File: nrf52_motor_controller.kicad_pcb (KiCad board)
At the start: 2 copper layers, 56 x 26.5 mm, 50 parts, among them J1 Screw_Terminal_01x04, J2 Conn_01x12, J3 Conn_01x12, Q1 AO3400A, SW1 SW_Push, SW2 SW_Push, U1 HT7533, U2 nRF52832-QFAA, U3 DRV8876PWPT, Y1 32MHz, Y2 32.768kHz

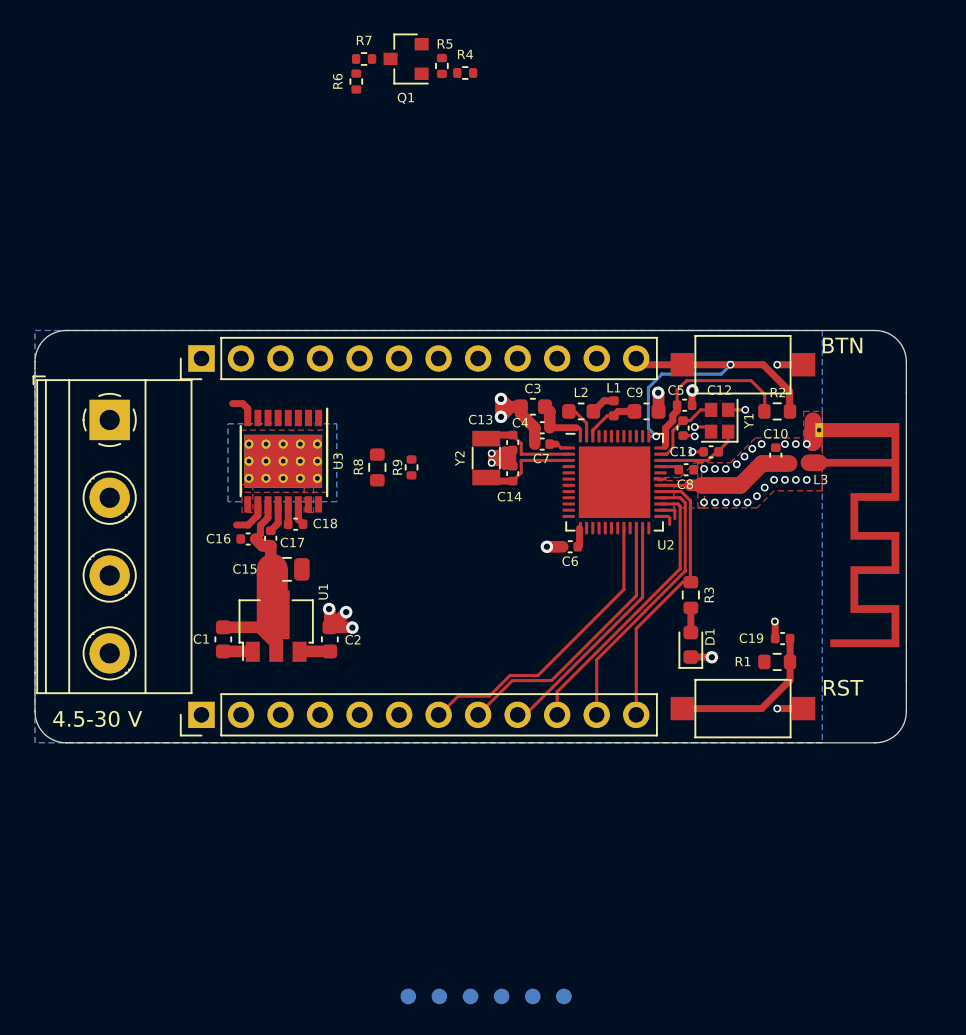
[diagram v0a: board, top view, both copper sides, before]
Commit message: Replace 12 pin headers with 10 pin
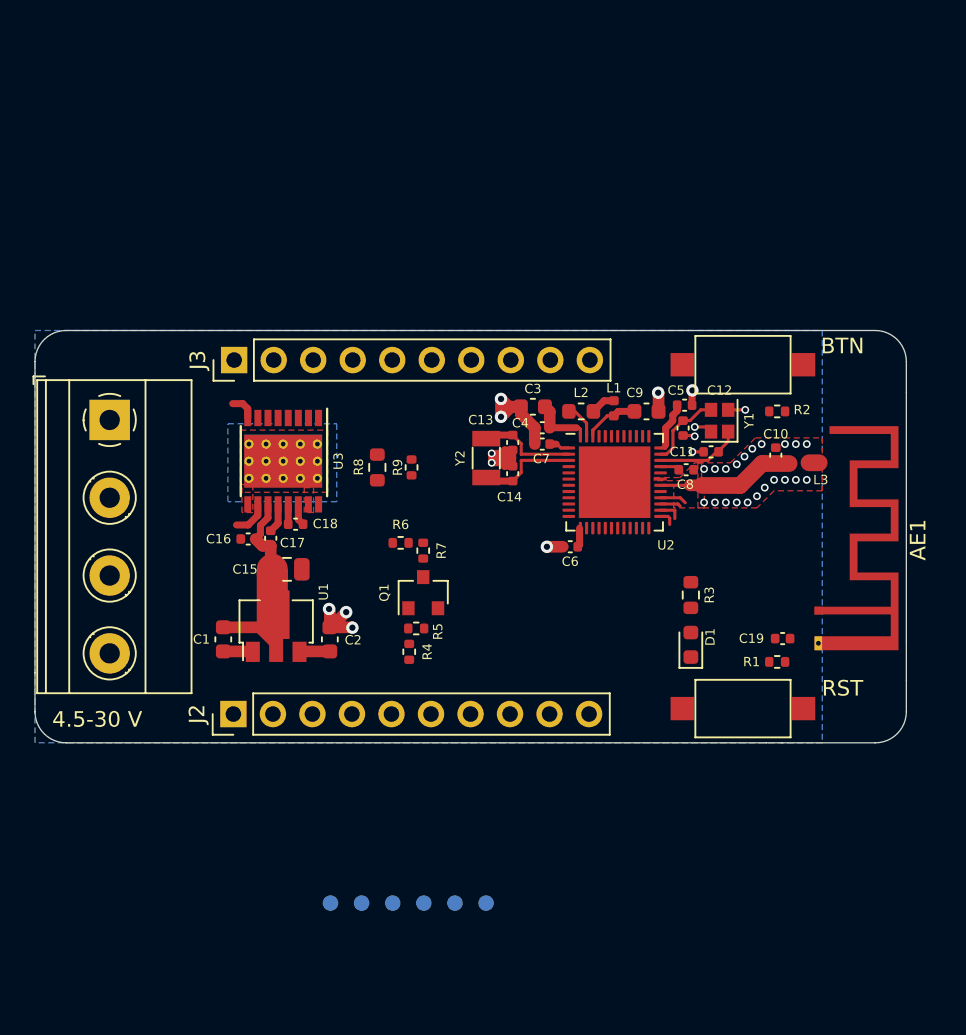
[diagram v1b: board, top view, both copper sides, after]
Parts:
- AE1: footprint RF_Antenna:Texas_SWRA117D_2.4GHz_Right -> RF_Antenna:Texas_SWRA117D_2.4GHz_Left
- J2, J3: value Conn_01x12 -> Conn_01x10; footprint Connector_PinHeader_2.54mm:PinHeader_1x12_P2.54mm_Vertical -> Connector_PinHeader_2.54mm:PinHeader_1x10_P2.54mm_Vertical
- R1, R2: footprint Resistor_SMD:R_0603_1608Metric -> Resistor_SMD:R_0402_1005Metric
- moved R4 37.4 mm to (142.1, 105.7), turned to 270 degrees
- moved R5 36.2 mm to (142.5, 104.2), turned to 0 degrees
- moved Q1 34.3 mm to (142.9, 101.8), turned to 90 degrees
- moved R7 31.8 mm to (142.9, 99.2), turned to 270 degrees
- moved R6 29.8 mm to (141.5, 98.7), turned to 0 degrees
- moved AE1 9.50 mm to (168.3, 103.0)
- moved TP1 7.81 mm to (137.0, 121.8)
- moved TP2 7.81 mm to (139.0, 121.8)
- moved TP3 7.81 mm to (141.0, 121.8)
- moved TP4 7.81 mm to (143.0, 121.8)
- moved TP5 7.81 mm to (145.0, 121.8)
- moved TP6 7.81 mm to (147.0, 121.8)
- moved J3 2.10 mm to (130.8, 86.9)
- moved J2 2.05 mm to (130.8, 109.7)
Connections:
- net /OUT1 renamed /OUT+
- net /OUT2 renamed /OUT-
- J3 pad 10: /GPIO27 -> /GPIO26
- J3 pad 3: (no net) -> /GPIO9
- J3 pad 4: /GPIO9 -> /GPIO10
- J3 pad 5: /GPIO10 -> /GPIO31
- J3 pad 6: /GPIO31 -> /GPIO30
- J3 pad 7: /GPIO30 -> /GPIO29
- J3 pad 8: /GPIO29 -> /GPIO28
- J3 pad 9: /GPIO28 -> /GPIO27
- U2 pad 28: /GPIO23 -> /GPIO_LED
- U2 pad 29: /GPIO_LED -> (no net)
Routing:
- net /GPIO_BTN: track 21.7 -> 0.00 mm, vias 2 -> 0
- net /GPIO17: track 19.2 -> 0.00 mm
- net /GPIO23: track 17.7 -> 0.00 mm
- net /GPIO19: track 17.7 -> 0.00 mm
- net /GPIO22: track 18.0 -> 1.33 mm
- net /GPIO_LED: track 17.7 -> 1.73 mm
- net /GPIO20: track 15.6 -> 0.00 mm
- net /~RESET: track 10.4 -> 0.00 mm
- net GND: track 37.0 -> 28.5 mm, vias 39 -> 35
- net +3V3: track 18.9 -> 10.5 mm
- net Net-(D1-Pad2): track 1.59 -> 0.00 mm
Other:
- board text added: "OUT+"
- board text added: "OUT-"
- board text removed: "OUT1"
- board text removed: "OUT2"

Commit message: Add custom test point symbol and footprint for 1.27 mm pitch TP
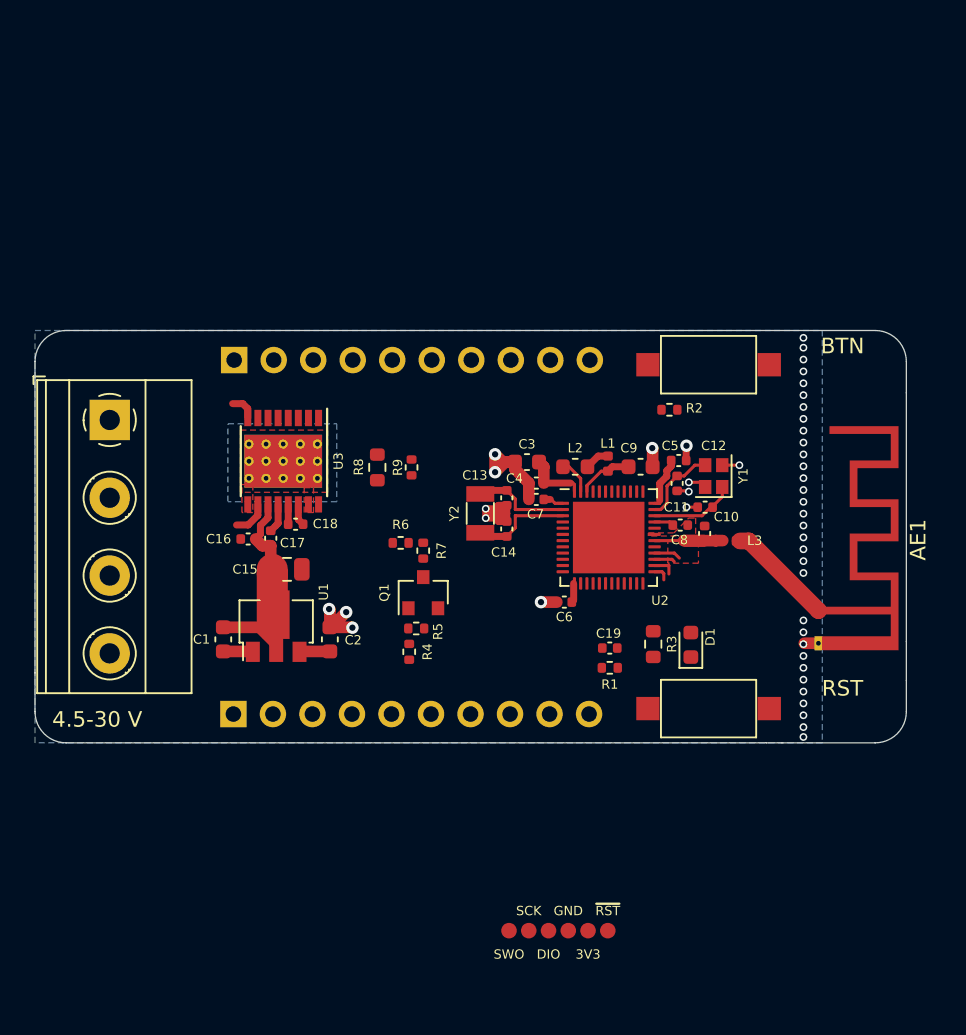
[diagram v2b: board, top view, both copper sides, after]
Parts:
- J2, J3: moved to B.Cu
- TP1: value VTref -> Test_point_1mm; footprint TestPoint:TestPoint_Pad_D1.0mm -> custom_footprints:test_point_1mm; moved to F.Cu
- TP2: value SWDIO -> Test_point_1mm; footprint TestPoint:TestPoint_Pad_D1.0mm -> custom_footprints:test_point_1mm; moved to F.Cu
- TP3: value SWDCLK -> Test_point_1mm; footprint TestPoint:TestPoint_Pad_D1.0mm -> custom_footprints:test_point_1mm; moved to F.Cu
- TP4: value SWO -> Test_point_1mm; footprint TestPoint:TestPoint_Pad_D1.0mm -> custom_footprints:test_point_1mm; moved to F.Cu
- TP5: value ~RESET -> Test_point_1mm; footprint TestPoint:TestPoint_Pad_D1.0mm -> custom_footprints:test_point_1mm; moved to F.Cu
- TP6: value GND -> Test_point_1mm; footprint TestPoint:TestPoint_Pad_D1.0mm -> custom_footprints:test_point_1mm; moved to F.Cu
- moved TP1 16.6 mm to (153.5, 123.6)
- moved TP2 12.1 mm to (151.0, 123.6)
- moved C19 11.1 mm to (154.9, 105.4)
- moved R1 10.8 mm to (154.9, 106.7)
- moved TP5 9.98 mm to (154.8, 123.6)
- moved TP3 8.92 mm to (149.7, 123.6)
- moved R2 6.93 mm to (158.8, 90.1)
- moved C10 6.80 mm to (161.0, 98.0)
- moved L3 6.77 mm to (162.6, 98.5)
- moved TP4 5.75 mm to (148.5, 123.6)
- moved TP6 5.57 mm to (152.3, 123.6)
- moved R3 3.97 mm to (157.7, 105.2)
- moved C11 3.58 mm to (161.1, 96.4)
- moved C12 3.58 mm to (159.3, 94.8)
- moved C13 3.58 mm to (148.3, 95.8)
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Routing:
- net Net-(AE1-Pad1): track 0.66 -> 6.89 mm
- net Net-(C10-Pad1): track 8.51 -> 5.33 mm
- net GND: track 28.5 -> 29.4 mm, vias 35 -> 46
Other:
- board text added: "SCK"
- board text removed: "DCK"
